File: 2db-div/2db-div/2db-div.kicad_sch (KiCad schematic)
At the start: 34 parts, among them J1001 Conn_01x02, J1002 From R2, J1003 Conn_01x02, J1004 Conn_Coaxial, SW1001 2dB, SW1002 Video, U1001 MC1458

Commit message: v7 conversion
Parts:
- D1001: Spice_Lib_File 2db-div-spice\fairch.lib -> (none); Spice_Model 1N4152 -> (none); Spice_Netlist_Enabled Y -> (none); Spice_Node_Sequence 2 1 -> (none); Spice_Primitive D -> (none)
- H1001, H1002, H1003, H1004: value MountingHole -> ${SIM.PARAMS}; Spice_Netlist_Enabled N -> (none); Spice_Primitive R -> (none)
- J1001, J1003: Spice_Model Conn_01x02 -> (none); Spice_Netlist_Enabled N -> (none); Spice_Primitive J -> (none)
- J1002: Spice_Model From R2 -> (none); Spice_Netlist_Enabled N -> (none); Spice_Primitive J -> (none)
- J1004: Spice_Model Conn_Coaxial -> (none); Spice_Netlist_Enabled N -> (none); Spice_Primitive J -> (none)
- R1006: Spice_Lib_File 2db-div-spice\Pot.lib -> (none); Spice_Model pot_lin -> (none); Spice_Netlist_Enabled Y -> (none); Spice_Primitive X -> (none)
- R1012: Spice_Lib_File 2db-div-spice\Pot2.lib -> (none); Spice_Model pot_lin2 -> (none); Spice_Netlist_Enabled Y -> (none); Spice_Primitive X -> (none)
- SW1001: Spice_Model 2dB -> (none); Spice_Netlist_Enabled N -> (none); Spice_Primitive R -> (none)
- SW1002: value Video -> ${SIM.PARAMS}; Spice_Netlist_Enabled N -> (none); Spice_Primitive R -> (none)
- TP1001: value 1458 Pin 1 -> ${SIM.PARAMS}; Spice_Netlist_Enabled N -> (none)
- TP1002: value 1458 Pin 7 -> ${SIM.PARAMS}; Spice_Netlist_Enabled N -> (none)
- U1001: Spice_Lib_File 2db-div-spice\LM358-dual.lib -> (none); Spice_Model LM358c -> (none); Spice_Netlist_Enabled N -> (none); Spice_Primitive X -> (none)
- V1001: value +5 -> 5; Spice_Model dc 5 -> (none); Spice_Netlist_Enabled Y -> (none); Spice_Primitive V -> (none)
- V1002: Spice_Model dc -15 -> (none); Spice_Netlist_Enabled Y -> (none); Spice_Primitive V -> (none)
- V1003: value +15 -> 15; Spice_Model dc 15 -> (none); Spice_Netlist_Enabled Y -> (none); Spice_Primitive V -> (none)

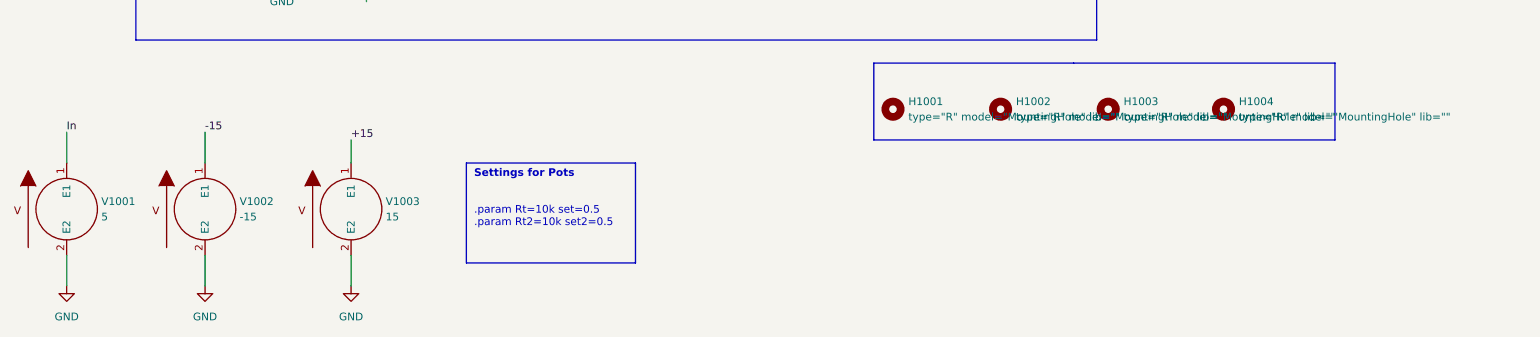
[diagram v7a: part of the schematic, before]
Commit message: 2nd div board tweaks
Updated component symbols
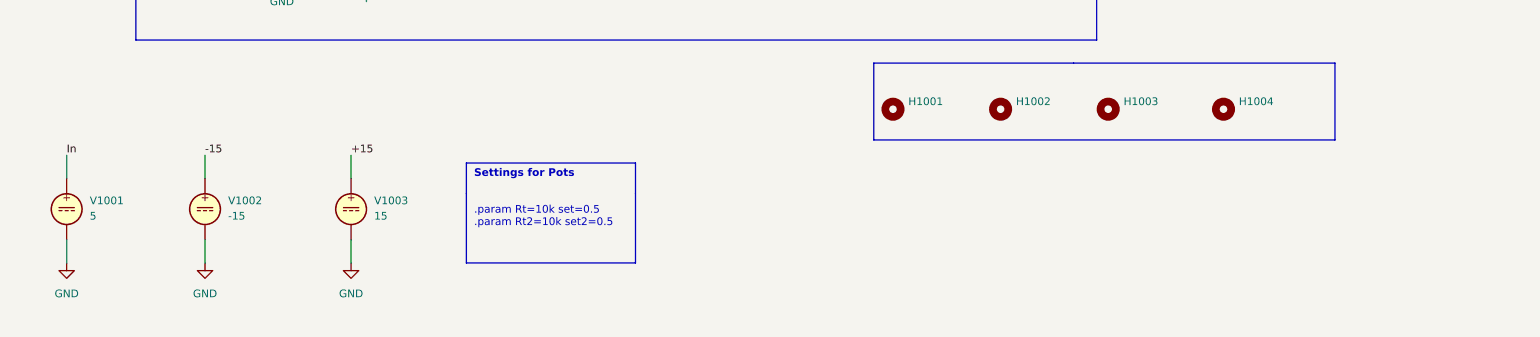
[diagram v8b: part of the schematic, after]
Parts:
- J1002: symbol Connector:Conn_01x01_Female -> Connector:Conn_01x01_Socket
- V1001, V1002, V1003: symbol pspice:VSOURCE -> Simulation_SPICE:VDC; now in the parts list
